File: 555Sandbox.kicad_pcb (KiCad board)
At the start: 2 copper layers, 66.6 x 38 mm, 33 parts, among them J1 VIN, SW1 RESET, SW2 MODE, U1 NE555P, U2 LM3914N

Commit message: patch: minor silkscreen updates
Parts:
- moved D10 0.56 mm to (136.3, 92.2)
- moved D11 0.56 mm to (130.0, 95.4)
- moved D3 0.56 mm to (130.0, 70.6)
- moved D5 0.56 mm to (130.0, 76.8)
- moved D7 0.56 mm to (130.0, 83.0)
- moved D8 0.56 mm to (136.3, 86.0)
- moved D9 0.56 mm to (130.0, 89.2)
- moved R2 0.56 mm to (116.9, 89.6)
- moved R4 0.56 mm to (113.9, 82.0)
- moved R8 0.56 mm to (110.9, 89.6)
- moved U2 0.56 mm to (119.5, 72.1)
- moved D2 0.23 mm to (136.3, 67.4)
- moved D4 0.23 mm to (136.3, 73.6)
- moved D6 0.23 mm to (136.4, 79.8)
- moved REF** 0.16 mm to (117.0, 64.3)
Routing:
- net Net-(U2-SIG): track 5.45 -> 6.04 mm

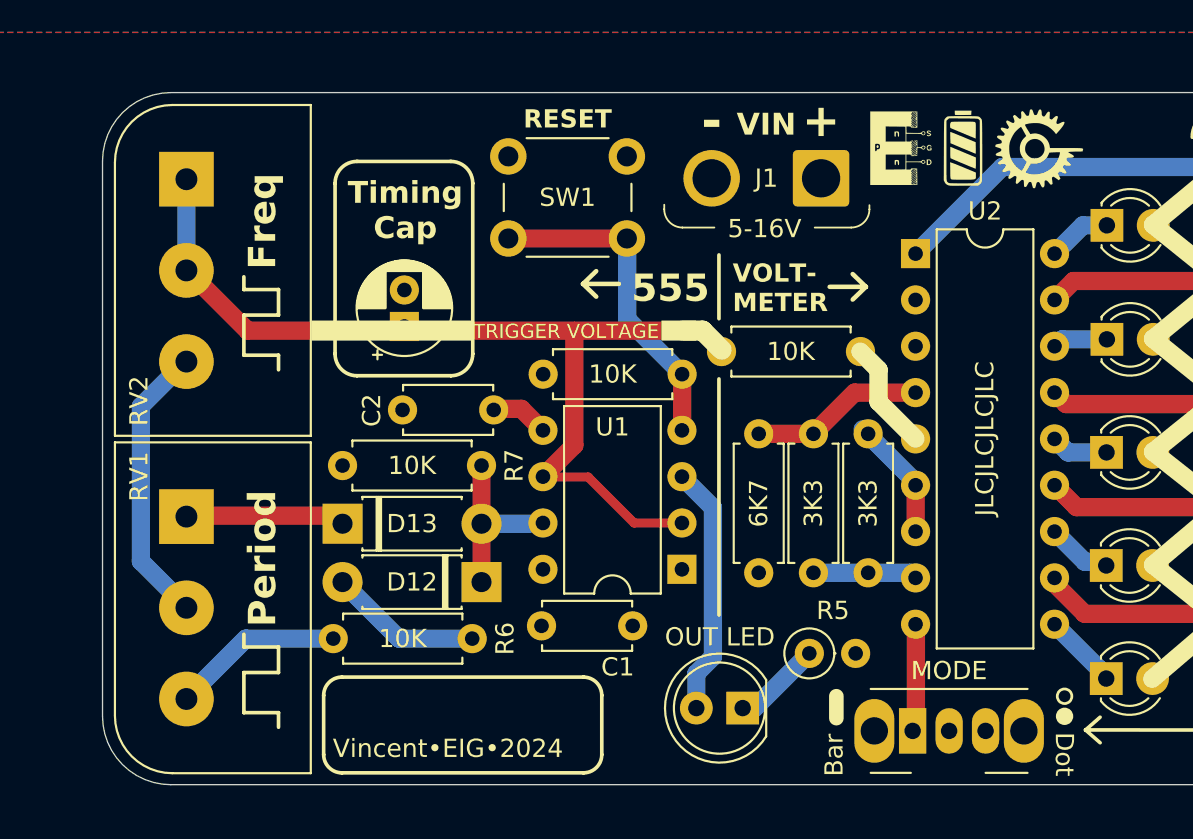
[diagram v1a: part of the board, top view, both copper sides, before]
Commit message: patch: split resistor into 2, update silkscreen
allow use of same resistor values instead of an additional 6k7 resistor
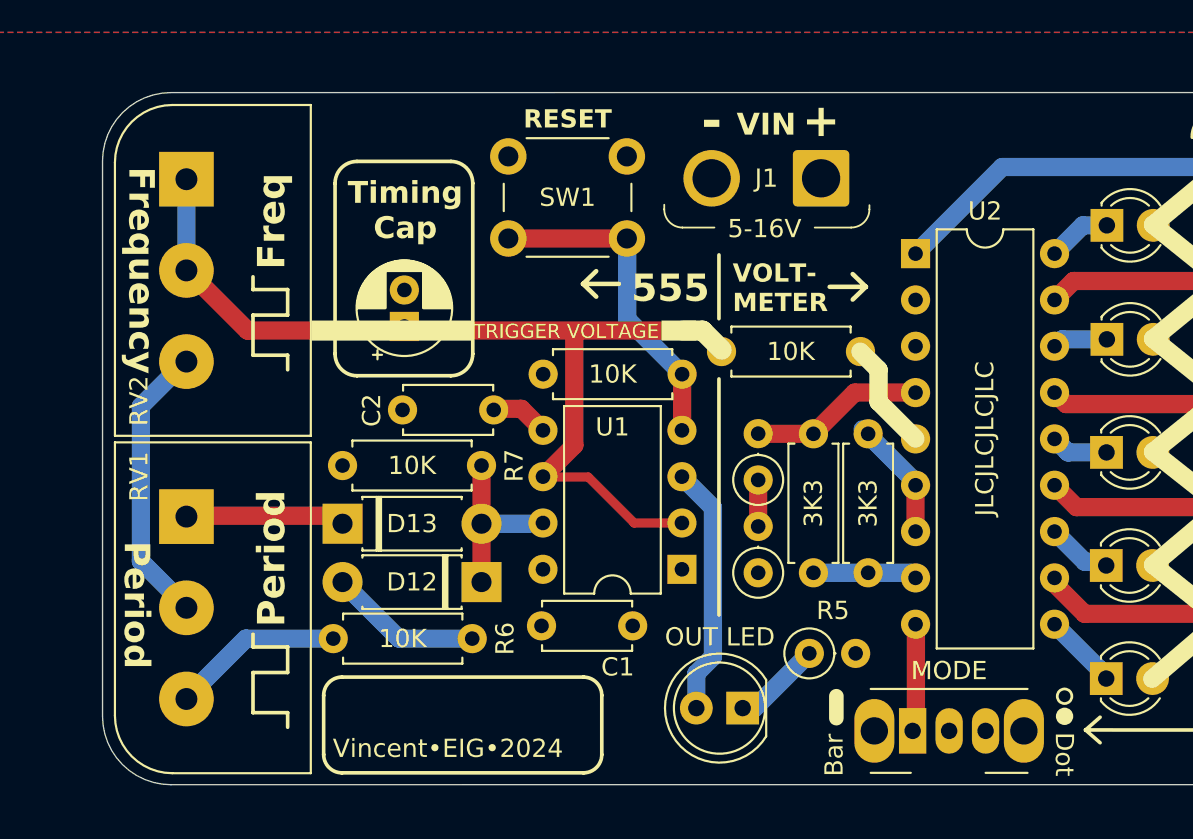
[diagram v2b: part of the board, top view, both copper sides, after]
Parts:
- removed REF**: EIG, footprints:EIG
- added R9: 3K3, Resistor_THT:R_Axial_DIN0207_L6.3mm_D2.5mm_P2.54mm_Vertical, F.Cu at (110.9, 84.5)
- R8: value 6K7 -> 3K3; footprint Resistor_THT:R_Axial_DIN0207_L6.3mm_D2.5mm_P7.62mm_Horizontal -> Resistor_THT:R_Axial_DIN0207_L6.3mm_D2.5mm_P2.54mm_Vertical
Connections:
- R8 pad 2: /Voltage Meter/RLO -> Net-(R8-Pad2)
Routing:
- net Net-(R8-Pad2): track 0.00 -> 2.55 mm
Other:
- board text added: "Frequency"

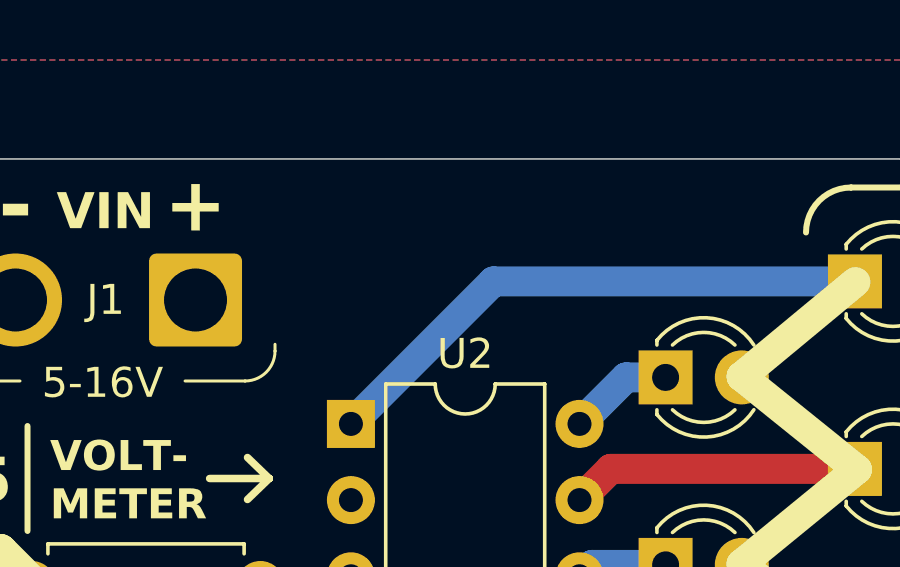
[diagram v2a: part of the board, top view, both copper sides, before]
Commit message: fix: replace missing EIG on silkscreen
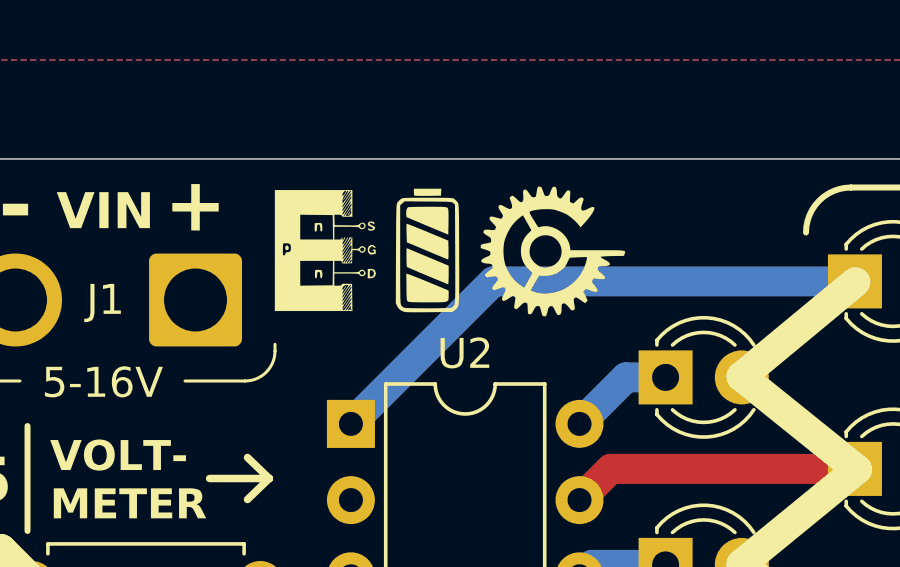
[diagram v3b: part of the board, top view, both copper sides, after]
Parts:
- added REF**: EIG, footprints:EIG, F.Cu at (117.0, 64.3)

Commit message: feat: board v1.4
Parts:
- removed D10, D11, D4, D5, D6, D7, D8, D9: LED, LED_THT:LED_D3.0mm
- removed D12, D13: 1N4001, Diode_THT:D_DO-41_SOD81_P7.62mm_Horizontal
- removed J1: VIN, Connector_Wire:SolderWire-1.5sqmm_1x02_P6mm_D1.7mm_OD3mm
- removed R1, R3: 10K, Resistor_THT:R_Axial_DIN0207_L6.3mm_D2.5mm_P7.62mm_Horizontal
- removed R2, R4: 3K3, Resistor_THT:R_Axial_DIN0207_L6.3mm_D2.5mm_P7.62mm_Horizontal
- removed R8, R9: 3K3, Resistor_THT:R_Axial_DIN0207_L6.3mm_D2.5mm_P2.54mm_Vertical
- removed SW2: MODE, Button_Switch_THT:SW_Slide_SPDT_Angled_CK_OS102011MA1Q
- removed U2: LM3914N, Package_DIP:DIP-18_W7.62mm
- added BT1: Battery_Cell, Battery:BatteryHolder_Keystone_3000_1x12mm, B.Cu at (90.4, 83.9)
- added G***: LOGO, NUSHSat:v1 burden bear, B.Cu at (86.5, 67.5)
- added H1: MountingHole_Pad, MountingHole:MountingHole_3mm_Pad, F.Cu at (93.2, 70.4)
- C1, C2: footprint Capacitor_THT:C_Disc_D4.7mm_W2.5mm_P5.00mm -> Capacitor_SMD:C_0603_1608Metric
- C3: value 10uF -> 4.7uF; footprint Capacitor_THT:CP_Radial_D5.0mm_P2.00mm -> Capacitor_SMD:CP_Elec_5x5.4
- D1: value OUT LED -> LED; footprint LED_THT:LED_D5.0mm -> LED_SMD:LED_PLCC_2835
- D2, D3: value LED -> 1N5819WS; footprint LED_THT:LED_D3.0mm -> Diode_SMD:D_SOD-323
- R5: value 200 -> 300; footprint Resistor_THT:R_Axial_DIN0207_L6.3mm_D2.5mm_P2.54mm_Vertical -> Resistor_SMD:R_0603_1608Metric
- R6, R7: footprint Resistor_THT:R_Axial_DIN0207_L6.3mm_D2.5mm_P7.62mm_Horizontal -> Resistor_SMD:R_0603_1608Metric
- RV1: value 100K -> 250K; footprint Potentiometer_THT:Potentiometer_Alps_RK163_Single_Horizontal -> Potentiometer_THT:Potentiometer_Runtron_RM-065_Vertical
- RV2: value 100K -> 1M; footprint Potentiometer_THT:Potentiometer_Alps_RK163_Single_Horizontal -> Potentiometer_THT:Potentiometer_Runtron_RM-065_Vertical
- SW1: value RESET -> SW_SPDT; footprint Button_Switch_THT:SW_PUSH_6mm_H4.3mm -> Button_Switch_THT:SW_Slide_SPDT_Angled_CK_OS102011MA1Q
- U1: value NE555P -> LMC555xM; footprint Package_DIP:DIP-8_W7.62mm -> Package_SO:SOIC-8_3.9x4.9mm_P1.27mm
- moved D2 51.9 mm to (87.2, 84.0), turned to -90 degrees
- moved D3 46.0 mm to (87.2, 87.2), turned to -90 degrees
- moved REF** 41.7 mm to (81.5, 86.2), turned to 90 degrees
- moved R5 26.8 mm to (94.3, 75.6), turned to 180 degrees
- moved D1 24.1 mm to (94.5, 78.6), turned to -90 degrees
- moved SW1 21.9 mm to (78.7, 78.5), turned to -90 degrees
- moved G*** 19.0 mm to (67.5, 78.7)
- moved U1 16.0 mm to (91.8, 83.6)
- moved C1 9.91 mm to (90.3, 87.8), turned to -90 degrees
- moved R6 9.59 mm to (86.3, 89.6)
- moved C2 9.40 mm to (87.0, 80.9), turned to 90 degrees
- moved R7 4.10 mm to (88.9, 87.8), turned to 90 degrees
- moved RV1 2.12 mm to (81.4, 87.6), turned to -90 degrees
- moved RV2 1.82 mm to (81.3, 68.3), turned to -90 degrees
- moved C3 1.78 mm to (89.9, 76.9)
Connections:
- D2 pad 2: VCC -> /DIS
- D3 pad 1: Net-(D3-K) -> /DIS
- D3 pad 2: VCC -> Net-(D3-A)
- R6 pad 1: Net-(D13-A) -> Net-(D3-A)
- RV1 pad 1: Net-(D12-K) -> Net-(D2-K)
- SW1 pad 1: GND -> Net-(BT1-+)
- SW1 pad 2: /RST -> VCC
- U1 pad 4: /RST -> VCC
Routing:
- net VCC: track 0.00 -> 36.9 mm, vias 0 -> 3
- net Net-(BT1-+): track 0.00 -> 28.1 mm
- net /TRIG: track 53.5 -> 31.2 mm
- net /RST: track 18.4 -> 0.00 mm
- net Net-(D2-K): track 18.8 -> 7.60 mm
- net Net-(D10-K): track 10.3 -> 0.00 mm
- net Net-(D8-K): track 9.70 -> 0.00 mm
- net Net-(D4-K): track 9.61 -> 0.00 mm
- net Net-(D6-K): track 9.42 -> 0.00 mm
- net /Voltage Meter/RLO: track 9.23 -> 0.00 mm
- net Net-(D12-K): track 8.74 -> 0.00 mm
- net /OUT: track 13.8 -> 5.10 mm
- net Net-(D13-A): track 8.39 -> 0.00 mm
- net /Voltage Meter/REF: track 6.81 -> 0.00 mm
- net Net-(U2-SIG): track 6.04 -> 0.00 mm
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- added copper zone on F.Cu, net /OUT
- added copper zone on B.Cu, net GND
- removed copper zone on B.Cu, net VCC
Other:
- board size 66.6 x 38 mm -> 21.8 x 27.1 mm
- board text added: "Designed by Vincent"
- board text added: "NUSH DSAP 2024"
- board text added: "NUSH•EIG•2024"
- board text added: "ON"
- board text added: "POWER"
- board text removed: "+"
- board text removed: "-"
- board text removed: "5-16V"
- board text removed: "555"
- board text removed: "555Sandbox"
- board text removed: "Bar"
- board text removed: "CAP VOLTMETER"
- board text removed: "Dot"
- board text removed: "Frequency"
- board text removed: "JLCJLCJLCJLC"
- board text removed: "TRIGGER VOLTAGE"
- board text removed: "Timing Cap"
- board text removed: "VOLT- METER"
- board text removed: "Vincent•EIG•2024"

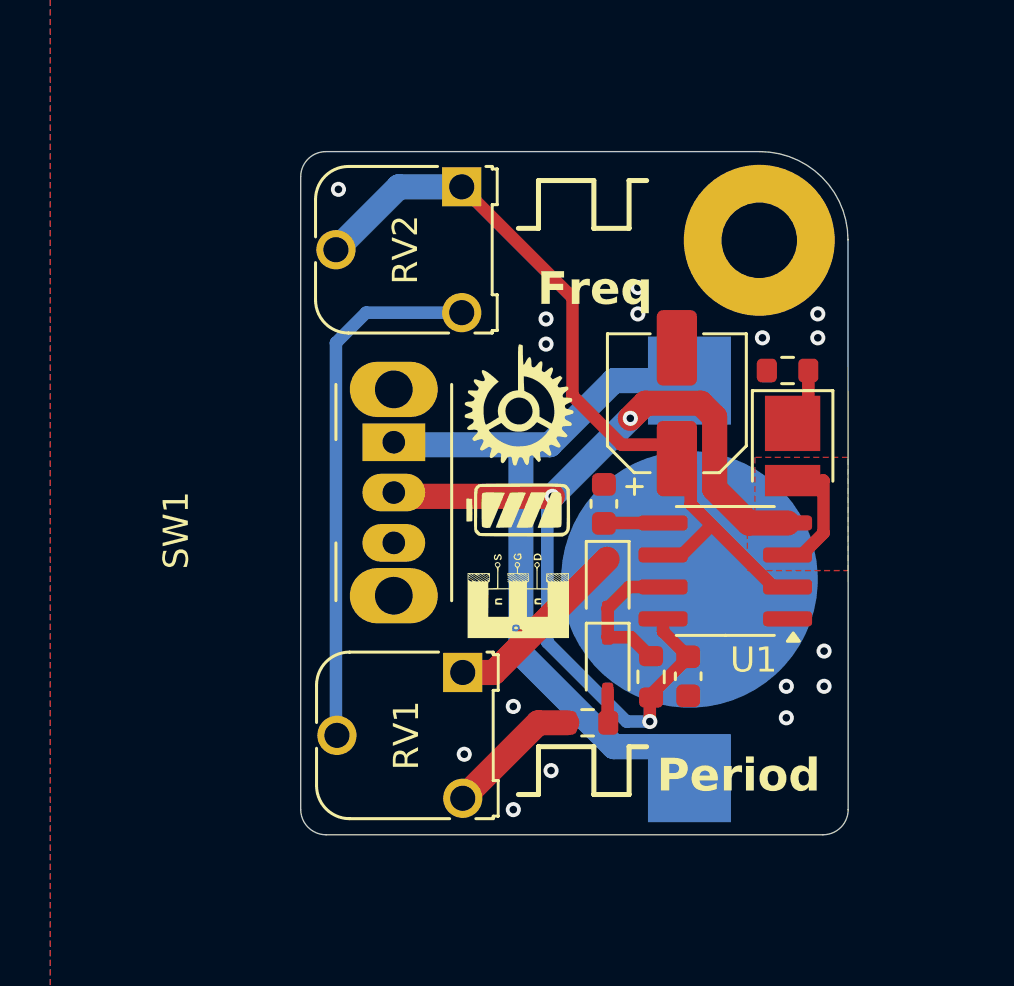
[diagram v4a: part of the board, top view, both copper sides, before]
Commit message: feat: microcontroller based v2.1
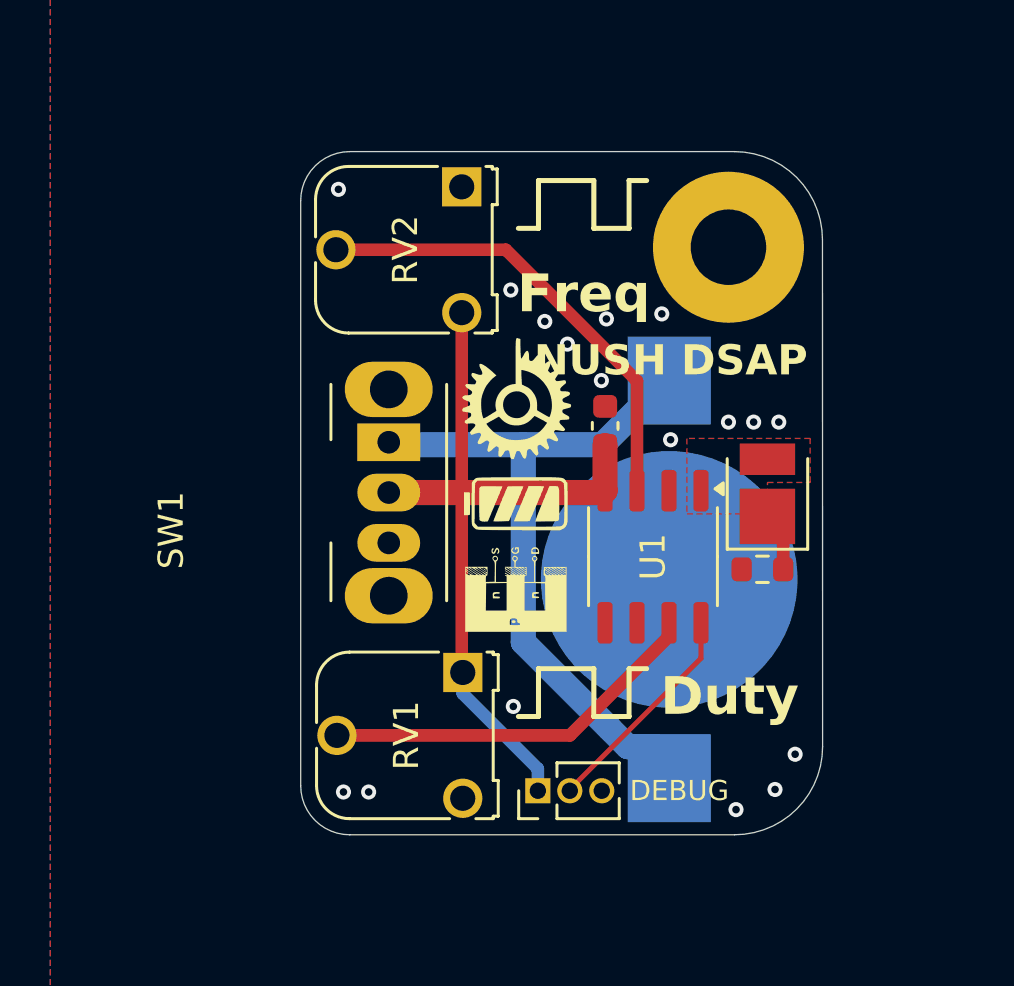
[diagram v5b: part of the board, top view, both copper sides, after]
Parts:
- removed C2: 0.1uF, Capacitor_SMD:C_0603_1608Metric
- removed C3: 4.7uF, Capacitor_SMD:CP_Elec_5x5.4
- removed D2, D3: 1N5819WS, Diode_SMD:D_SOD-323
- removed R6, R7: 10K, Resistor_SMD:R_0603_1608Metric
- added J1: DEBUG, Connector_PinHeader_1.27mm:PinHeader_1x03_P1.27mm_Vertical, F.Cu at (84.4, 92.3)
- R5: value 300 -> 200
- RV1: value 250K -> 1M
- U1: value LMC555xM -> CH32V003JxMx; footprint Package_SO:SOIC-8_3.9x4.9mm_P1.27mm -> Package_SO:SOP-8_3.9x4.9mm_P1.27mm
- moved C1 10.5 mm to (87.0, 77.8), turned to 90 degrees
- moved R5 7.96 mm to (93.3, 83.5)
- moved U1 2.93 mm to (89.0, 83.0), turned to -90 degrees
- moved D1 2.15 mm to (93.5, 80.5), turned to 90 degrees
- moved H1 1.26 mm to (92.0, 70.7)
- moved BT1 0.81 mm to (89.6, 83.9)
- moved G*** 0.46 mm to (86.4, 67.0), turned to 0 degrees
- moved REF** 0.27 mm to (81.5, 86.0)
- moved SW1 0.20 mm to (78.5, 78.5)
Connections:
- net Net-(BT1-+) renamed +BATT
- RV1 pad 1: Net-(D2-K) -> VCC
- RV1 pad 2: Net-(RV1-Pad2) -> /DUTY
- RV1 pad 3: Net-(R6-Pad2) -> GND
- RV2 pad 1: /TRIG -> GND
- RV2 pad 2: /TRIG -> /FREQ
- RV2 pad 3: Net-(RV1-Pad2) -> VCC
- U1 pad 1: GND -> /OUT
- U1 pad 2: /TRIG -> GND
- U1 pad 3: /OUT -> /FREQ
- U1 pad 5: Net-(U1-CV) -> unconnected-(U1-PC1-Pad5)
- U1 pad 6: /TRIG -> unconnected-(U1-PC2-Pad6)
- U1 pad 7: /DIS -> /DUTY
- U1 pad 8: VCC -> /SWIO
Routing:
- net /TRIG: track 31.2 -> 0.00 mm
- net Net-(RV1-Pad2): track 21.1 -> 0.00 mm
- net /FREQ: track 0.00 -> 18.5 mm
- net /DUTY: track 0.00 -> 15.4 mm
- net /SWIO: track 0.00 -> 8.63 mm
- net Net-(D2-K): track 7.60 -> 0.00 mm
- net VCC: track 36.9 -> 30.8 mm, vias 3 -> 0
- net /DIS: track 5.71 -> 0.00 mm
- net Net-(R6-Pad2): track 5.38 -> 0.00 mm
- net /OUT: track 5.10 -> 0.00 mm
- net Net-(U1-CV): track 2.36 -> 0.00 mm
- net Net-(D3-A): track 1.25 -> 0.00 mm
- net +BATT: track 28.1 -> 27.1 mm
- net GND: vias 16 -> 17
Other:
- board size 21.8 x 27.1 mm -> 20.7 x 27.1 mm
- board text added: "2024"
- board text added: "Designed"
- board text added: "Duty"
- board text added: "More Info:"
- board text added: "NUSH DSAP"
- board text added: "VDD SWIO VSS"
- board text added: "Vincent"
- board text added: "by"
- board text added: "i.vkwok.dev/ dp24"
- board text removed: "Designed by Vincent"
- board text removed: "NUSH DSAP 2024"
- board text removed: "Period"
